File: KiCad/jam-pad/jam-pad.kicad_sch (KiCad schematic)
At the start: 62 parts, among them J1 USB_C, J2 PH_01x03_2.54mm, SW1 MX_Hotswap, SW10 MX_Hotswap, SW11 MX_Hotswap, SW12 MX_Hotswap, SW13 SW_Push, SW14 RotaryEncoder_Switch, SW15 SW_Push, SW2 MX_Hotswap, SW3 MX_Hotswap, SW4 MX_Hotswap, SW5 MX_Hotswap, SW6 MX_Hotswap, SW7 MX_Hotswap, SW8 MX_Hotswap, SW9 MX_Hotswap, U1 RP2040, U2 OLED_RGB_128x128_waveshare, U3 W25Q16JVSNIQ, U4 MIC5319-3.3YD5, Y1 ECS-120-18-33-JGN

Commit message: initial layout
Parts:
- SW14: footprint Rotary_Encoder:RotaryEncoder_Alps_EC11E-Switch_Vertical_H20mm -> Keebio-Parts:RotaryEncoder_Alps_EC11E-Switch_Vertical_H20mm
- U1: footprint jackrabbit:RP2040-QFN-56_HandSoldering -> jam-pad:RP2040-QFN-56_HandSoldering
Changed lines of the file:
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@@
     (property "Reference" "U1" (id 0) (at 158.75 137.16 0))
     (property "Value" "RP2040" (id 1) (at 212.09 236.22 0))
-    (property "Footprint" "jackrabbit:RP2040-QFN-56_HandSoldering" (id 2) (at 168.91 186.69 0)
+    (property "Footprint" "jam-pad:RP2040-QFN-56_HandSoldering" (id 2) (at 168.91 186.69 0)
       (effects (font (size 1.27 1.27)) hide)
     )
@@
     (property "Reference" "SW14" (id 0) (at 322.58 165.2102 0))
     (property "Value" "RotaryEncoder_Switch" (id 1) (at 322.58 167.7471 0))
-    (property "Footprint" "Rotary_Encoder:RotaryEncoder_Alps_EC11E-Switch_Vertical_H20mm" (id 2) (at 318.77 169.926 0)
+    (property "Footprint" "Keebio-Parts:RotaryEncoder_Alps_EC11E-Switch_Vertical_H20mm" (id 2) (at 318.77 169.926 0)
       (effects (font (size 1.27 1.27)) hide)
     )
@@
     )
     (path "/efb321da-8384-4118-a41b-6508be470393"
-      (reference "SW14") (unit 1) (value "RotaryEncoder_Switch") (footprint "Rotary_Encoder:RotaryEncoder_Alps_EC11E-Switch_Vertical_H20mm")
+      (reference "SW14") (unit 1) (value "RotaryEncoder_Switch") (footprint "Keebio-Parts:RotaryEncoder_Alps_EC11E-Switch_Vertical_H20mm")
     )
     (path "/da79fde2-9656-4d98-ba04-84a092367b96"
@@
     )
     (path "/63dc5db1-8abb-4175-974e-e0f00b8ce6ce"
-      (reference "U1") (unit 1) (value "RP2040") (footprint "jackrabbit:RP2040-QFN-56_HandSoldering")
+      (reference "U1") (unit 1) (value "RP2040") (footprint "jam-pad:RP2040-QFN-56_HandSoldering")
     )
     (path "/121f6c4b-b828-4bc1-9cfa-ef4ecc4fc396"

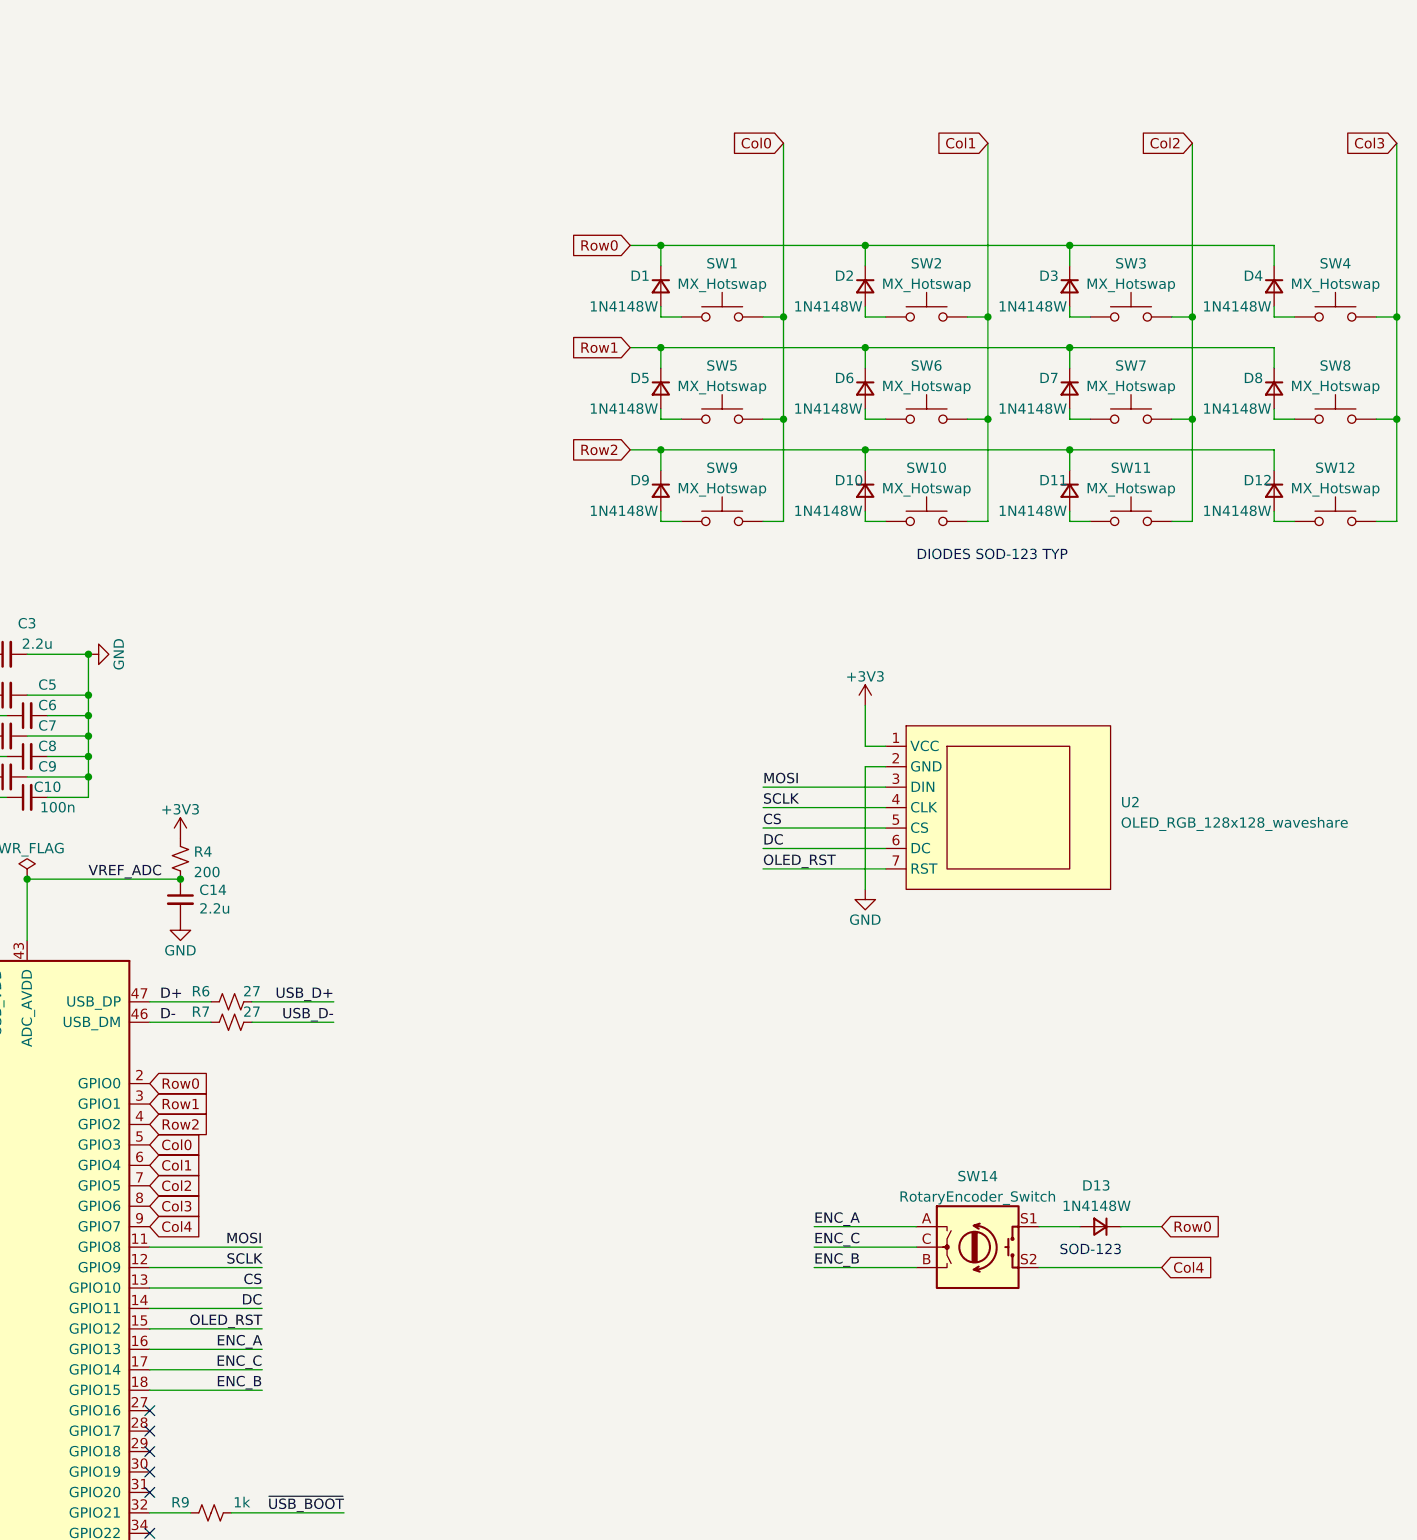
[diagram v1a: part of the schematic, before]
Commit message: 12 to 9 keys
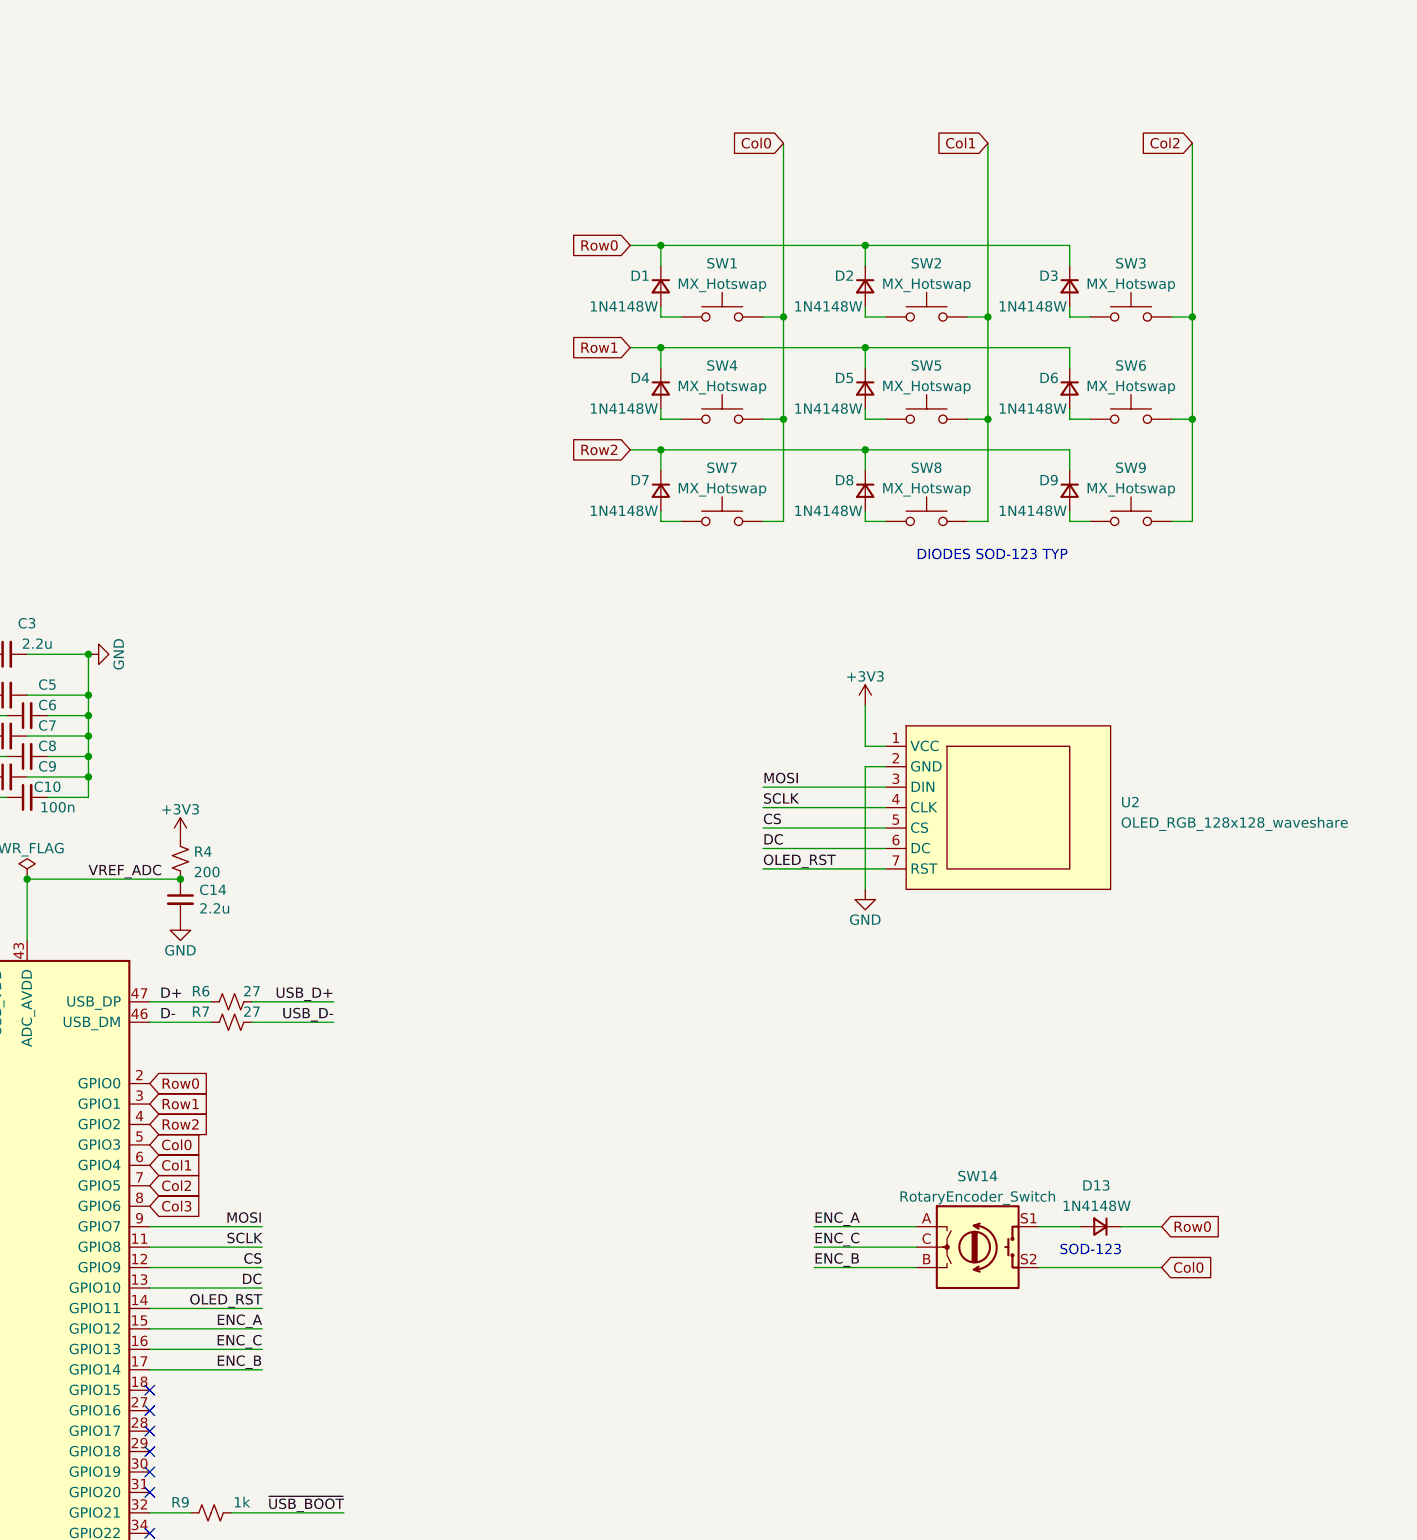
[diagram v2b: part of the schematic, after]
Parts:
- removed D12, D4, D8: 1N4148W, Diode_SMD:D_SOD-123, symbol Device:D_Small
- removed SW12, SW4, SW8: MX_Hotswap, MX_Only:MXOnly-1U-Hotswap-LED, symbol Switch:SW_Push
- renumbered D5 to D4, D6 to D5, D7 to D6, D9 to D7, D10 to D8, D11 to D9, SW5 to SW4, SW6 to SW5, SW7 to SW6, SW9 to SW7, SW10 to SW8, SW11 to SW9
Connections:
- net CS: now also U1.12 (GPIO9); no longer U1.13 (GPIO10)
- net Col0: now also SW14.S2
- net DC: now also U1.13 (GPIO10); no longer U1.14 (GPIO11)
- net ENC_A: now also U1.15 (GPIO12); no longer U1.16 (GPIO13)
- net ENC_B: now also U1.17 (GPIO14); no longer U1.18 (GPIO15)
- net ENC_C: now also U1.16 (GPIO13); no longer U1.17 (GPIO14)
- net MOSI: now also U1.9 (GPIO7); no longer U1.11 (GPIO8)
- net OLED_RST: now also U1.14 (GPIO11); no longer U1.15 (GPIO12)
- net SCLK: now also U1.11 (GPIO8); no longer U1.12 (GPIO9)
- removed net Col4: SW14.S2, U1.9 (GPIO7)
- no-connect marks 16 -> 17

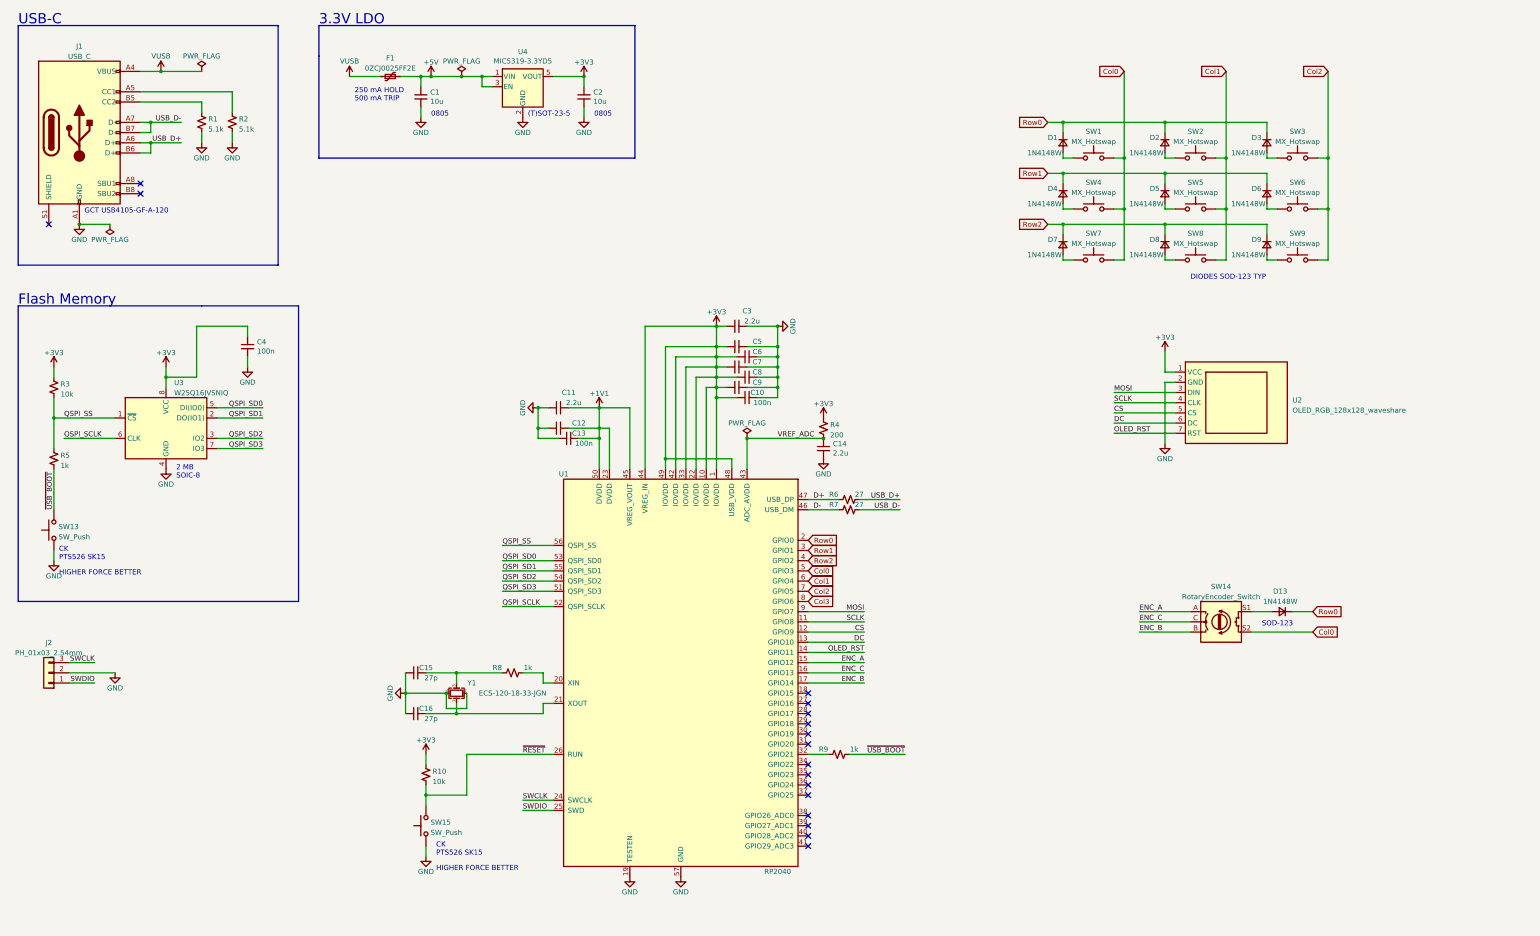
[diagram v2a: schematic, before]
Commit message: added multi part sym for switch+led, remove backups
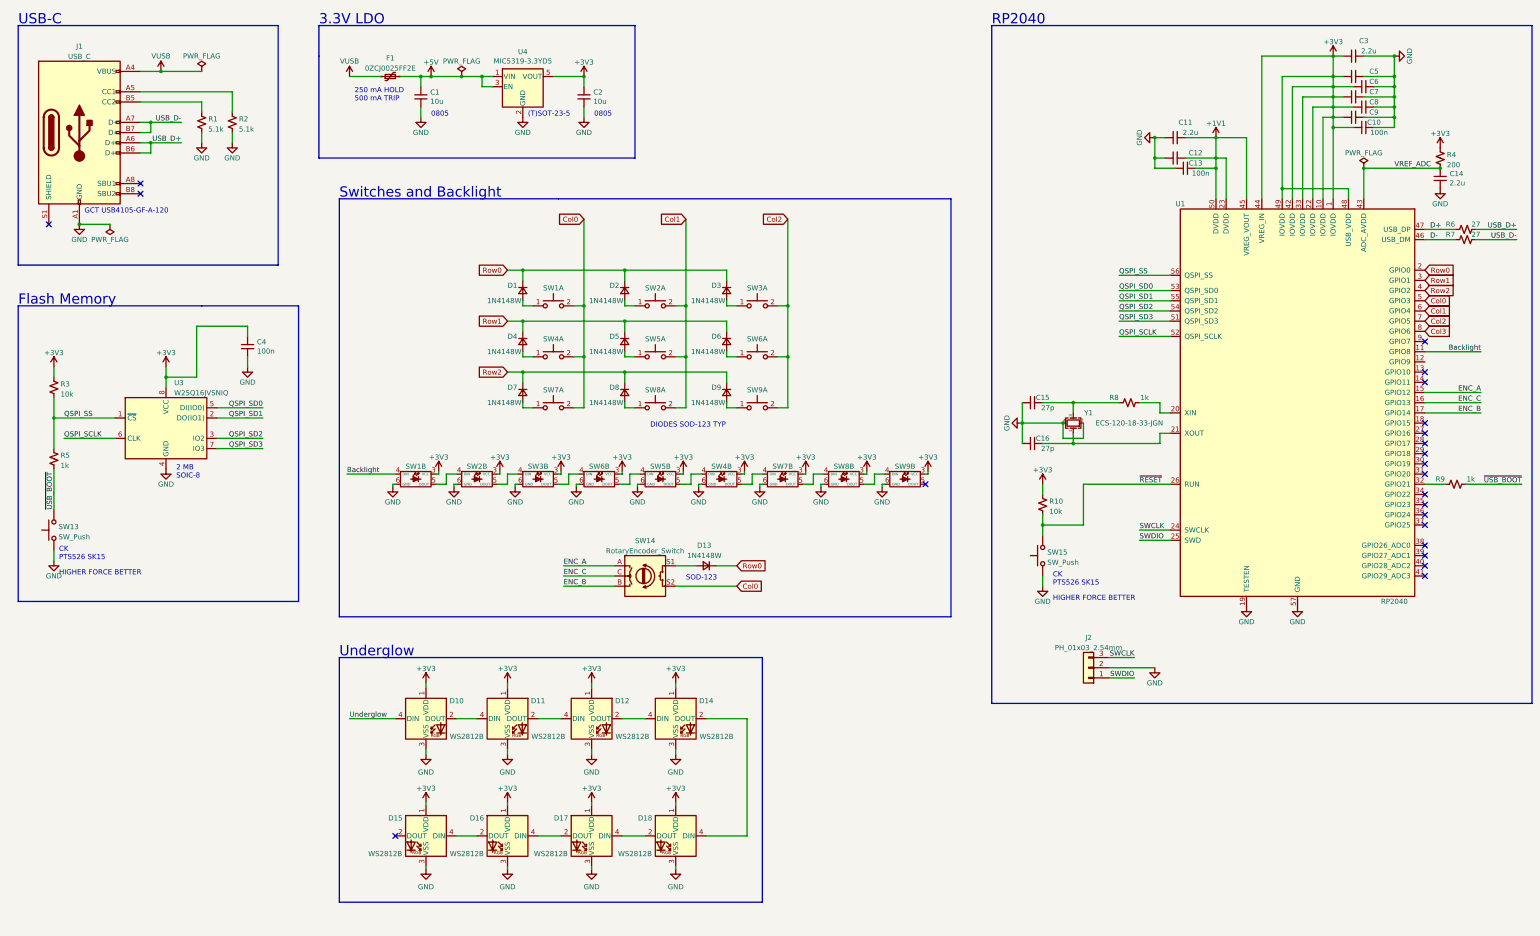
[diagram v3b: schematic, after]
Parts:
- removed SW1, SW2, SW3, SW4, SW5, SW6, SW7, SW8, SW9: MX_Hotswap, MX_Only:MXOnly-1U-Hotswap-LED, symbol Switch:SW_Push
- removed U2: OLED_RGB_128x128_waveshare, jam-pad:Display_Waveshare_OLED_1.5inch_128x128, symbol jam-pad:OLED_RGB_128x128_waveshare
- added D10, D11, D12, D14, D15, D16, D17, D18: WS2812B, LED_SMD:LED_WS2812B_PLCC4_5.0x5.0mm_P3.2mm, symbol LED:WS2812B
- added SW1, SW2, SW3, SW4, SW5, SW6, SW7, SW8, SW9: MX_Hotswap_LED_RGB, jam-pad:MXOnly-1U-Hotswap-SK6812MINI-E, symbol jam-pad:MX_Hotswap_LED_RGB
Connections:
- net +3V3: now also D10.1 (VDD), D11.1 (VDD), D12.1 (VDD), D14.1 (VDD), D15.1 (VDD), D16.1 (VDD), D17.1 (VDD), D18.1 (VDD), SW1.3 (VCC), SW2.3 (VCC), SW3.3 (VCC), SW4.3 (VCC), SW5.3 (VCC), SW6.3 (VCC), SW7.3 (VCC), SW8.3 (VCC), SW9.3 (VCC)
- net Col0: now also SW1.2, SW4.2, SW7.2
- net Col1: now also SW2.2, SW5.2, SW8.2
- net Col2: now also SW3.2, SW6.2, SW9.2
- net GND: now also D10.3 (VSS), D11.3 (VSS), D12.3 (VSS), D14.3 (VSS), D15.3 (VSS), D16.3 (VSS), D17.3 (VSS), D18.3 (VSS), SW1.6 (GND), SW2.6 (GND), SW3.6 (GND), SW4.6 (GND), SW5.6 (GND), SW6.6 (GND), SW7.6 (GND), SW8.6 (GND), SW9.6 (GND)
- net at D6.2 (A): now also SW6.1
- net at D3.2 (A): now also SW3.1
- net at D4.2 (A): now also SW4.1
- net at D2.2 (A): now also SW2.1
- net at D5.2 (A): now also SW5.1
- net at D9.2 (A): now also SW9.1
- net at D7.2 (A): now also SW7.1
- net at D8.2 (A): now also SW8.1
- net at D1.2 (A): now also SW1.1
- net CS: no longer names the net of U1.12 (GPIO9)
- net DC: no longer names the net of U1.13 (GPIO10)
- net MOSI: no longer names the net of U1.9 (GPIO7)
- net OLED_RST: no longer names the net of U1.14 (GPIO11)
- net SCLK renamed Backlight
- net Backlight: now also SW1.4 (DIN)
- new net: D17.4 (DIN), D18.2 (DOUT)
- new net: D14.2 (DOUT), D18.4 (DIN)
- new net: D10.2 (DOUT), D11.4 (DIN)
- new net: SW8.5 (DOUT), SW9.4 (DIN)
- new net: SW3.5 (DOUT), SW6.4 (DIN)
- new net: SW5.4 (DIN), SW6.5 (DOUT)
- new net: D12.2 (DOUT), D14.4 (DIN)
- new net: D11.2 (DOUT), D12.4 (DIN)
- new net: SW1.5 (DOUT), SW2.4 (DIN)
- new net: SW2.5 (DOUT), SW3.4 (DIN)
- new net: SW4.4 (DIN), SW5.5 (DOUT)
- new net: SW7.5 (DOUT), SW8.4 (DIN)
- new net: SW4.5 (DOUT), SW7.4 (DIN)
- new net: D16.4 (DIN), D17.2 (DOUT)
- new net: D15.4 (DIN), D16.2 (DOUT)
- new net Underglow: D10.4 (DIN)
- no-connect marks 17 -> 22
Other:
- note added: "RP2040"
- note added: "Switches and Backlight"
- note added: "Underglow"
- moved on the sheet: C10, C11, C12, C13, C14, C15, C16, C3, C5, C6, C7, C8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
